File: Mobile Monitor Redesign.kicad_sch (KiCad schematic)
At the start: 45 parts, among them J1 Conn_01x02_Pin, J2 Conn_01x08_Pin, J3 Conn_01x08_Pin, J5 Conn_02x03_Odd_Even, J6 Micro_SD_Card_Det1, J7 Conn_01x05_Pin, J8 Conn_01x06_Socket, Q1 2N7002, Q2 AO3401A, U1 ATmega2560-16A, U11 TPL5010, U2 DS3232M, U3 AP2112K-3.3, U4 L80-R, U7 CH340C, Y1 Crystal

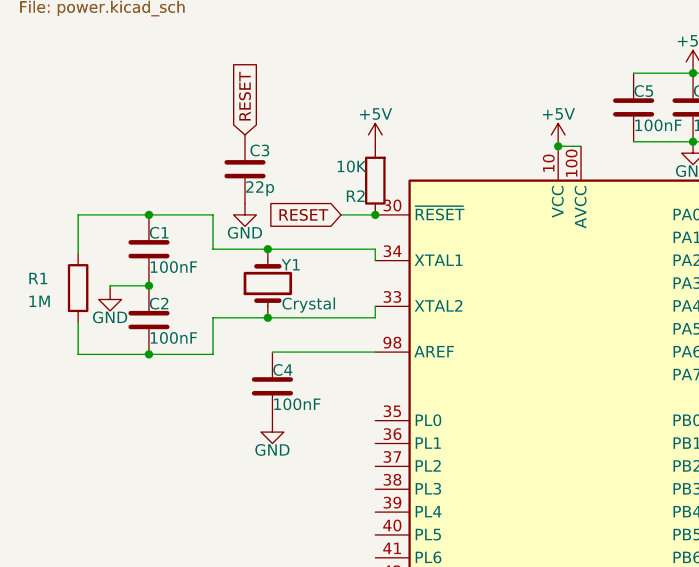
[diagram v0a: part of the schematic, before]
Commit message: cleaned up more routing and component placement
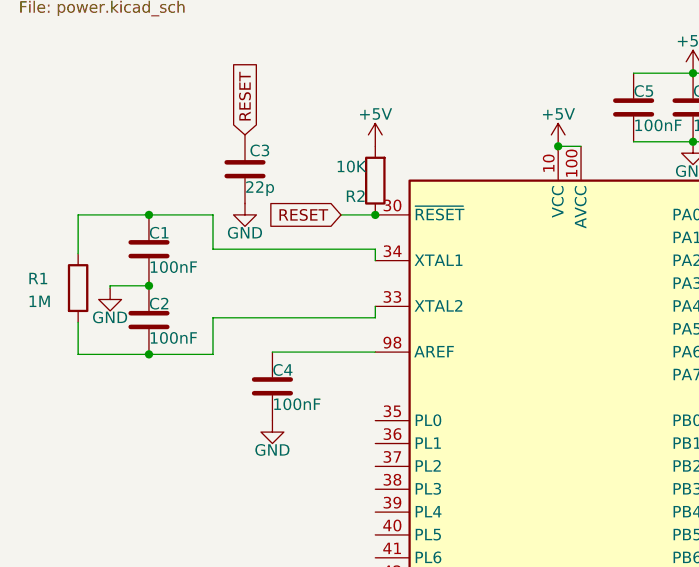
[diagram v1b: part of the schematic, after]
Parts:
- removed Y1: Crystal, Crystal:Crystal_HC50_Vertical, symbol Device:Crystal
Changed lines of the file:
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@@
-	)
-	(junction
-		(at 40.386 56.388)
-		(diameter 0)
-		(color 0 0 0 0)
 	)
 	(junction
@@
 	)
 	(junction
-		(at 40.386 64.008)
-		(diameter 0)
-		(color 0 0 0 0)
-	)
-	(junction
 		(at 52.324 52.578)
 		(diameter 0)
@@
 	(wire
 		(pts
-			(xy 52.324 56.388) (xy 40.386 56.388)
+			(xy 34.29 56.388) (xy 52.324 56.388)
 		)
 		(stroke
@@
 	(wire
 		(pts
-			(xy 52.324 64.008) (xy 40.386 64.008)
-		)
-		(stroke
-			(width 0)
-			(type default)
-		)
-	)
-	(wire
-		(pts
 			(xy 159.766 49.276) (xy 150.622 49.276)
 		)
@@
 	(wire
 		(pts
-			(xy 34.29 64.008) (xy 40.386 64.008)
+			(xy 34.29 64.008) (xy 52.324 64.008)
 		)
 		(stroke
@@
 		(pts
 			(xy 247.142 149.098) (xy 252.476 149.098)
-		)
-		(stroke
-			(width 0)
-			(type default)
-		)
-	)
-	(wire
-		(pts
-			(xy 34.29 56.388) (xy 40.386 56.388)
 		)
 		(stroke
@@
 					(unit 1)
 				)
-			)
-		)
-	)
-	(symbol
-		(lib_id "Device:Crystal")
-		(at 40.386 60.198 90)
-		(unit 1)
-		(exclude_from_sim no)
-		(in_bom yes)
-		(on_board yes)
-		(dnp no)
-		(property "Reference" "Y1"
-			(at 41.91 58.166 90)
-			(effects
-				(font
-					(size 1.27 1.27)
-				)
-				(justify right)
-			)
-		)
-		(property "Value" "Crystal"
-			(at 41.91 62.484 90)
-			(effects
-				(font
-					(size 1.27 1.27)
-				)
-				(justify right)
-			)
-		)
-		(property "Footprint" "Crystal:Crystal_HC50_Vertical"
-			(at 40.386 60.198 0)
-			(effects
-				(font
-					(size 1.27 1.27)
-				)
-				(hide yes)
-			)
-		)
-		(property "Datasheet" "~"
-			(at 40.386 60.198 0)
-			(effects
-				(font
-					(size 1.27 1.27)
-				)
-				(hide yes)
-			)
-		)
-		(property "Description" "Two pin crystal"
-			(at 40.386 60.198 0)
-			(effects
-				(font
-					(size 1.27 1.27)
-				)
-				(hide yes)
-			)
-		)
-		(pin "1"
-		)
-		(pin "2"
-		)
-		(instances
-			(project ""
-				(path "/b7045867-46a9-42d4-b526-22005757f9bb"
-					(reference "Y1")
-					(unit 1)
-				)

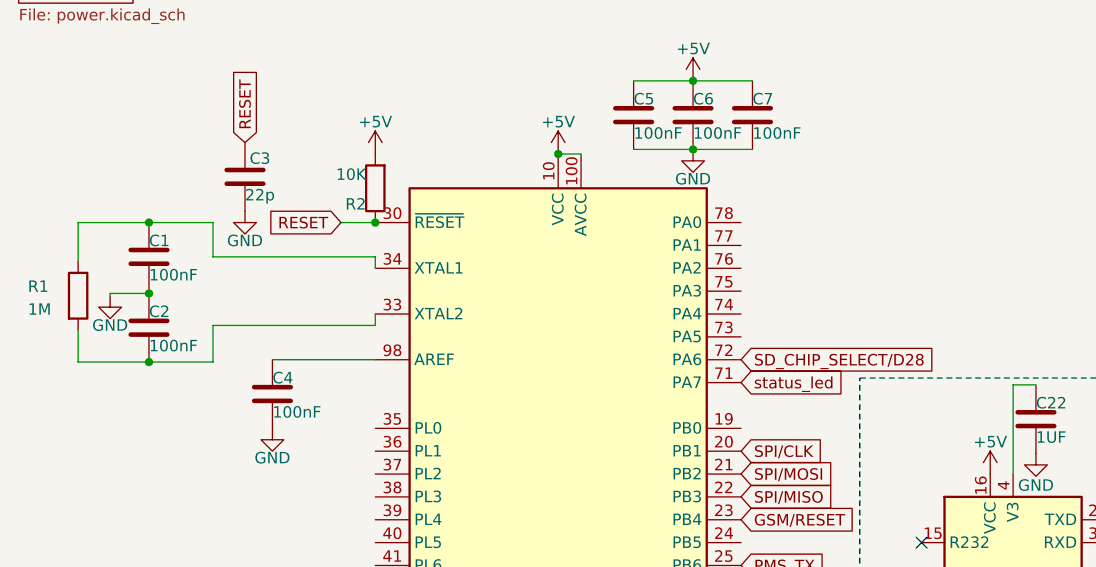
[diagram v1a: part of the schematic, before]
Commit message: routed the l80 gps daughter board and a few more modifications
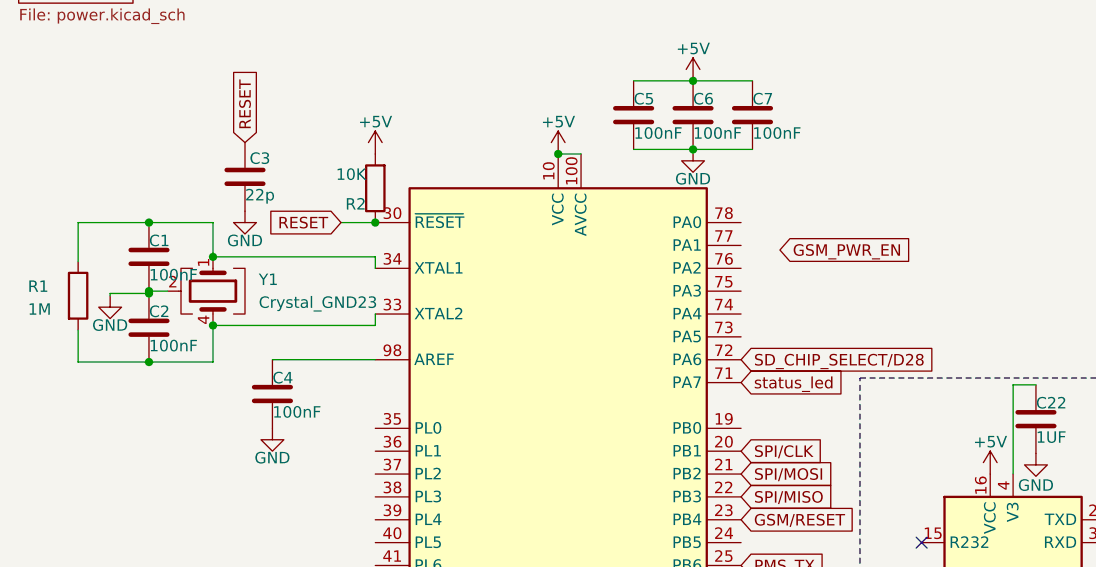
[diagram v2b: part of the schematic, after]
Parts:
- added Y1: Crystal_GND23, Crystal:Crystal_SMD_SeikoEpson_FA128-4Pin_2.0x1.6mm, symbol Device:Crystal_GND23
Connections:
- net GND: now also Y1.2 (G), Y1.3 (G)
- net at C1.1, R1.1, U1.34 (XTAL1): now also Y1.1
- net at C2.2, R1.2, U1.33 (XTAL2): now also Y1.4
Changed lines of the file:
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@@
 	)
 	(junction
+		(at 27.178 60.198)
+		(diameter 0)
+		(color 0 0 0 0)
+	)
+	(junction
+		(at 34.29 56.388)
+		(diameter 0)
+		(color 0 0 0 0)
+	)
+	(junction
 		(at 212.852 146.05)
 		(diameter 0)
@@
 	)
 	(junction
+		(at 34.29 64.008)
+		(diameter 0)
+		(color 0 0 0 0)
+	)
+	(junction
 		(at 155.702 148.082)
 		(diameter 0)
@@
 	(wire
 		(pts
-			(xy 27.178 60.452) (xy 27.178 60.198)
-		)
-		(stroke
-			(width 0)
-			(type default)
-		)
-	)
-	(wire
-		(pts
 			(xy 158.496 127.254) (xy 155.448 127.254)
 		)
@@
 	(wire
 		(pts
+			(xy 29.21 60.198) (xy 27.178 60.198)
+		)
+		(stroke
+			(width 0)
+			(type default)
+		)
+	)
+	(wire
+		(pts
 			(xy 220.472 138.43) (xy 220.472 137.922)
 		)
@@
 	(wire
 		(pts
+			(xy 27.178 60.198) (xy 27.178 60.452)
+		)
+		(stroke
+			(width 0)
+			(type default)
+		)
+	)
+	(wire
+		(pts
 			(xy 159.766 46.736) (xy 150.622 46.736)
 		)
@@
 		)
 	)
+	(global_label "GSM_PWR_EN"
+		(shape input)
+		(at 97.282 55.626 0)
+		(fields_autoplaced yes)
+		(effects
+			(font
+				(size 1.27 1.27)
+			)
+			(justify left)
+		)
+		(property "Intersheetrefs" "${INTERSHEET_REFS}"
+			(at 112.6042 55.626 0)
+			(effects
+				(font
+					(size 1.27 1.27)
+				)
+				(justify left)
+				(hide yes)
+			)
+		)
+	)
 	(global_label "PMS_RX"
 		(shape input)
@@
 					(unit 1)
 				)
+			)
+		)
+	)
+	(symbol
+		(lib_id "Device:Crystal_GND23")
+		(at 34.29 60.198 270)
+		(unit 1)
+		(exclude_from_sim no)
+		(in_bom yes)
+		(on_board yes)
+		(dnp no)
+		(fields_autoplaced yes)
+		(property "Reference" "Y1"
+			(at 39.37 58.9279 90)
+			(effects
+				(font
+					(size 1.27 1.27)
+				)
+				(justify left)
+			)
+		)
+		(property "Value" "Crystal_GND23"
+			(at 39.37 61.4679 90)
+			(effects
+				(font
+					(size 1.27 1.27)
+				)
+				(justify left)
+			)
+		)
+		(property "Footprint" "Crystal:Crystal_SMD_SeikoEpson_FA128-4Pin_2.0x1.6mm"
+			(at 34.29 60.198 0)
+			(effects
+				(font
+					(size 1.27 1.27)
+				)
+				(hide yes)
+			)
+		)
+		(property "Datasheet" "~"
+			(at 34.29 60.198 0)
+			(effects
+				(font
+					(size 1.27 1.27)
+				)
+				(hide yes)
+			)
+		)
+		(property "Description" "Four pin crystal, GND on pins 2 and 3"
+			(at 34.29 60.198 0)
+			(effects
+				(font
+					(size 1.27 1.27)
+				)
+				(hide yes)
+			)
+		)
+		(property private "KLC_S3.3" "The rectangle is not a symbol body but a graphical element"
+			(at 21.59 60.198 0)
+			(show_name yes)
+			(effects
+				(font
+					(size 1.27 1.27)
+				)
+				(hide yes)
+			)
+		)
+		(property private "KLC_S4.1" "Some pins are on 50mil grid to make the symbol small"
+			(at 19.05 60.198 0)
+			(show_name yes)
+			(effects
+				(font
+					(size 1.27 1.27)
+				)
+				(hide yes)
+			)
+		)
+		(pin "4"
+		)
+		(pin "1"
+		)
+		(pin "3"
+		)
+		(pin "2"
+		)
+		(instances
+			(project ""
+				(path "/b7045867-46a9-42d4-b526-22005757f9bb"
+					(reference "Y1")
+					(unit 1)
+				)

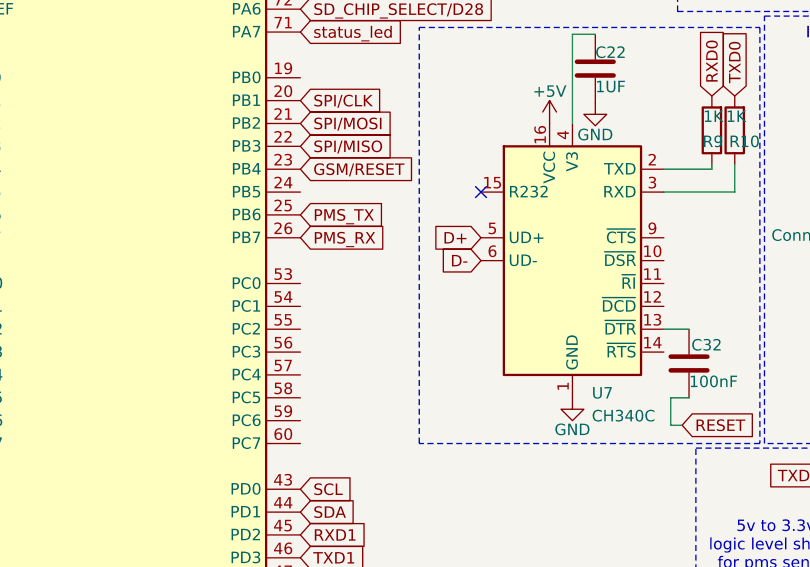
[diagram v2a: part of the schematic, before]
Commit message: updated routing and placement of devices on both PCBS
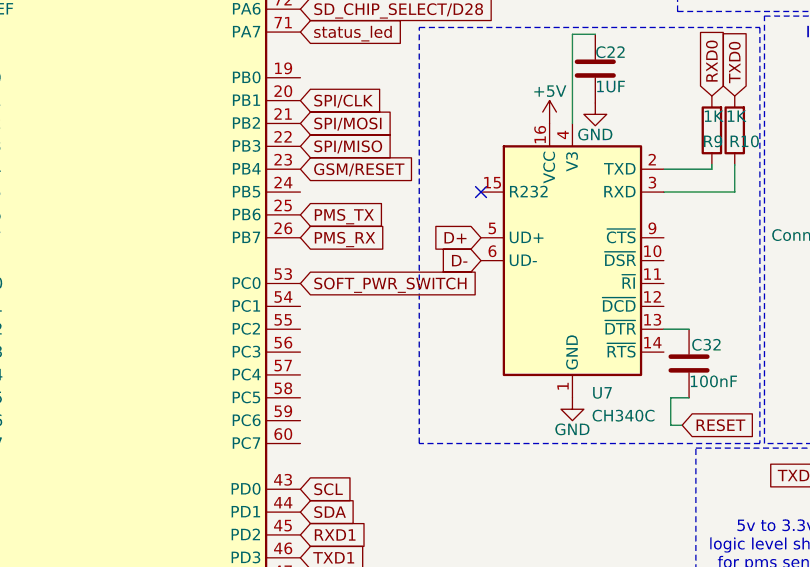
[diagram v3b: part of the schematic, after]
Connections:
- net SOFT_PWR_SWITCH: now also U1.53 (PC0)
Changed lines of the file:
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@@
+		)
+	)
+	(global_label "SOFT_PWR_SWITCH"
+		(shape input)
+		(at 92.964 98.298 0)
+		(fields_autoplaced yes)
+		(effects
+			(font
+				(size 1.27 1.27)
+			)
+			(justify left)
+		)
+		(property "Intersheetrefs" "${INTERSHEET_REFS}"
+			(at 113.3058 98.298 0)
+			(effects
+				(font
+					(size 1.27 1.27)
+				)
+				(justify left)
+				(hide yes)
+			)
 		)
 	)

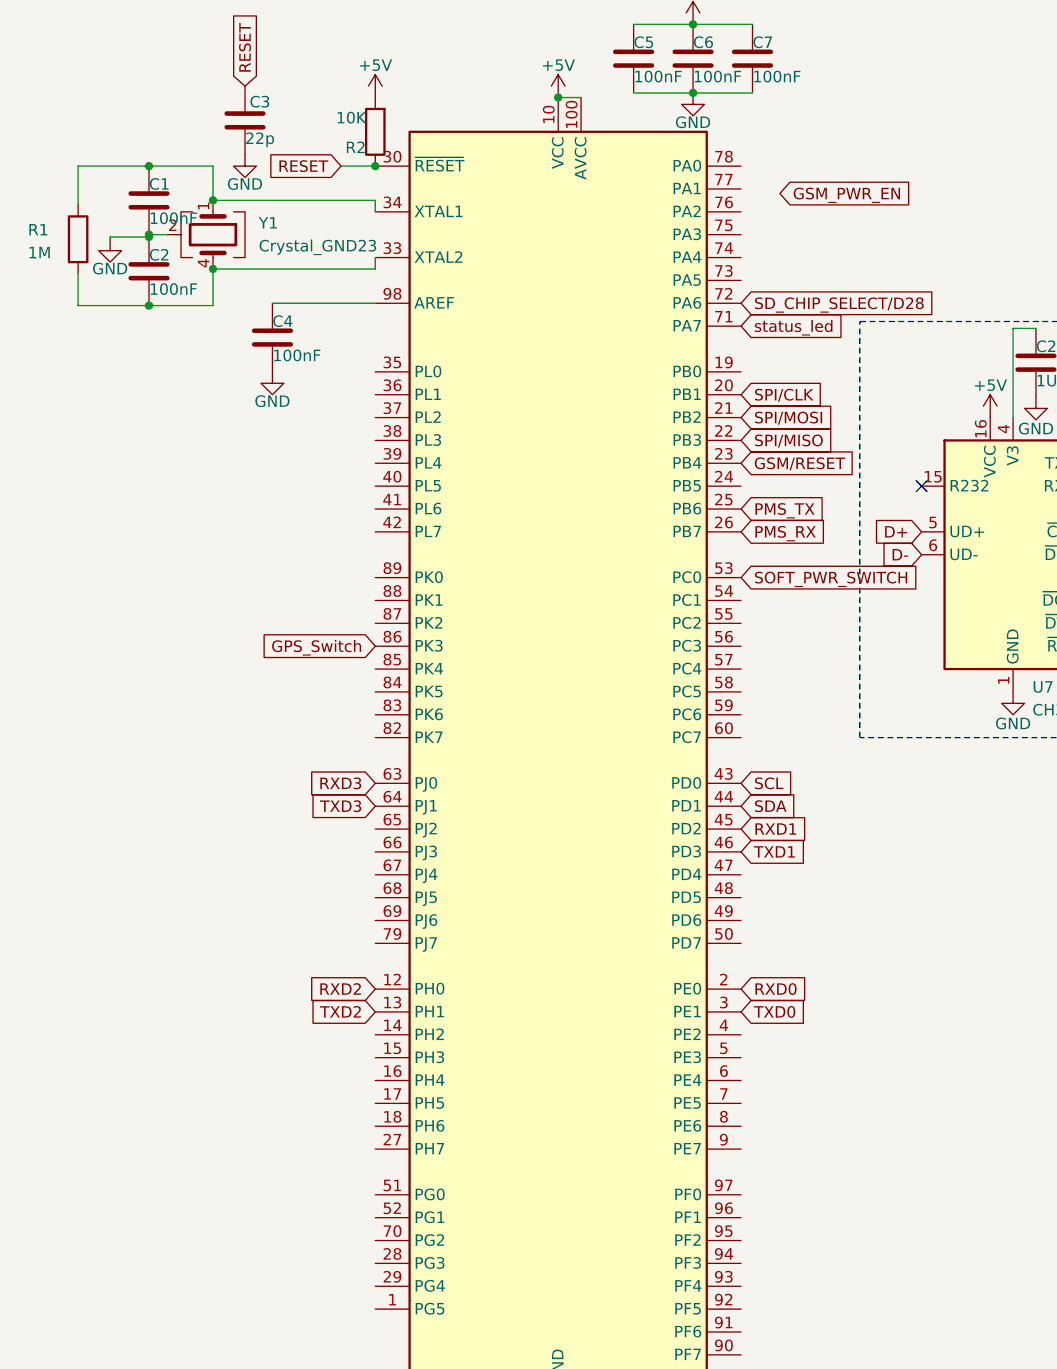
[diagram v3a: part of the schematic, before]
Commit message: adjusted file locations of some 3d models so that the project is fully localized
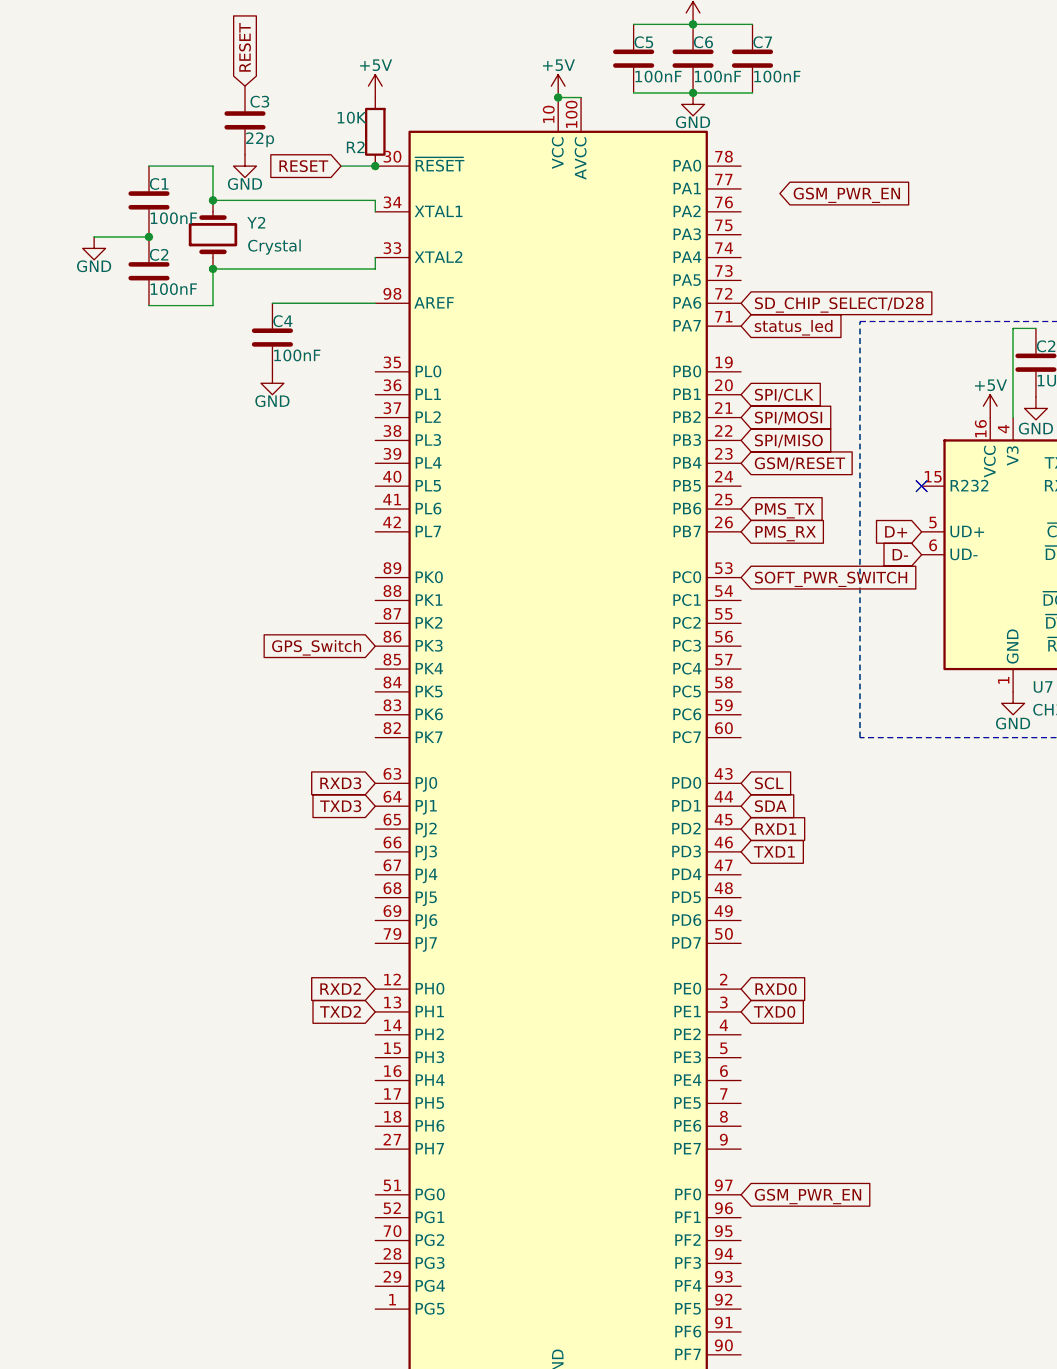
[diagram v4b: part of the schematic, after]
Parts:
- removed R1: 1M, Resistor_SMD:R_0603_1608Metric, symbol Device:R
- removed Y1: Crystal_GND23, Crystal:Crystal_SMD_SeikoEpson_FA128-4Pin_2.0x1.6mm, symbol Device:Crystal_GND23
- added Y2: Crystal, Crystal:Crystal_SMD_Abracon_ABM3-2Pin_5.0x3.2mm, symbol Device:Crystal
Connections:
- net GSM_PWR_EN: now also U1.97 (PF0)
- net at C1.1, U1.34 (XTAL1): now also Y2.2
- net at C2.2, U1.33 (XTAL2): now also Y2.1
